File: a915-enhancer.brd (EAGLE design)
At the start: 100 x 50 mm, 74 parts, among them U1 SCREW-M2X8, U10 FX2-20S-1.27DS, U2 SCREW-M2X8, U3 NUT-M2-SELFLOCK, U4 NUT-M2-SELFLOCK, U5 FX2-20P-1.27DS, U6 SCREW-M2X8, U7 SCREW-M2X8, U8 NUT-M2-SELFLOCK, U9 NUT-M2-SELFLOCK

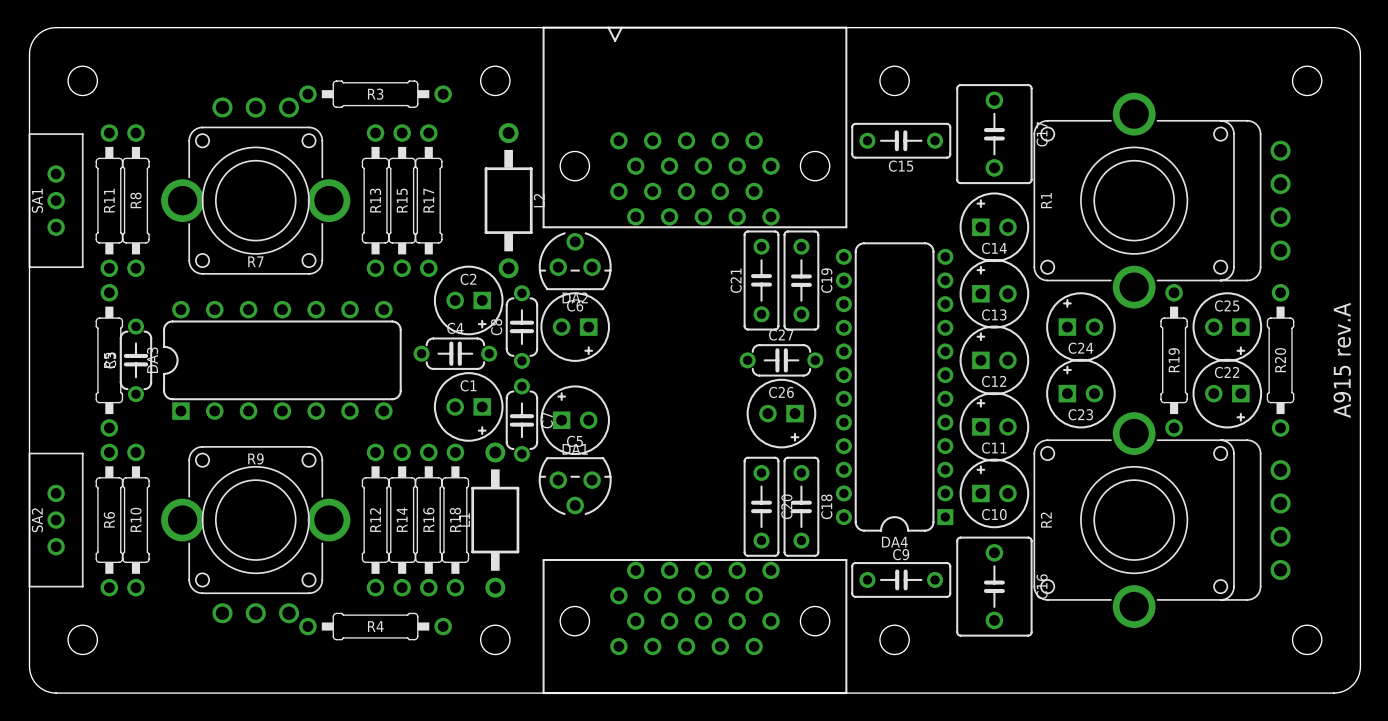
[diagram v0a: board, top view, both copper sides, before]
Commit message: A915a Change component placement
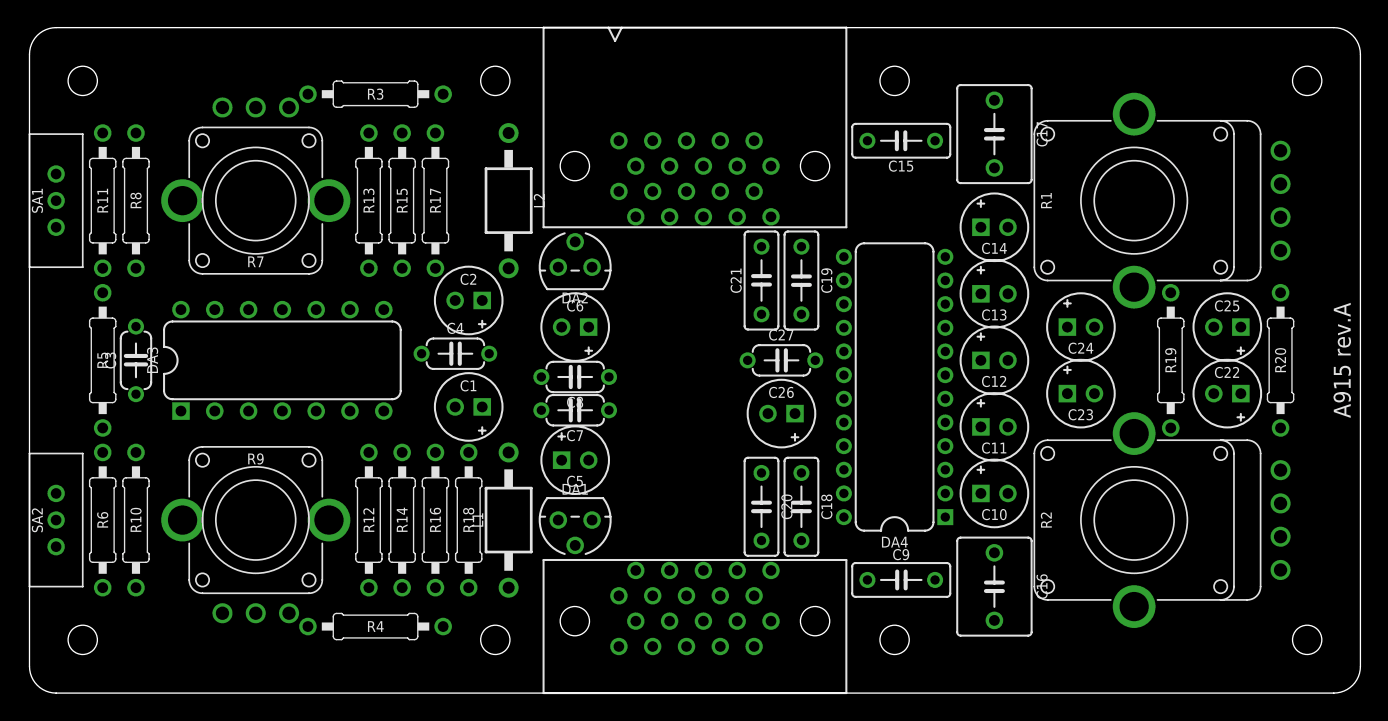
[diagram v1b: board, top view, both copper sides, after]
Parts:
- moved C8 5.48 mm to (41.0, 23.8), turned to 180 degrees
- moved C7 4.07 mm to (41.0, 21.2), turned to 180 degrees
- moved C5 3.00 mm to (41.0, 17.5)
- moved DA1 3.00 mm to (41.0, 13.0)
- moved L1 1.00 mm to (36.0, 13.0)
- moved R18 1.00 mm to (33.0, 13.0)
- moved R11 0.50 mm to (5.50, 37.0)
- moved R12 0.50 mm to (25.5, 13.0)
- moved R13 0.50 mm to (25.5, 37.0)
- moved R16 0.50 mm to (30.5, 13.0)
- moved R17 0.50 mm to (30.5, 37.0)
- moved R5 0.50 mm to (5.50, 25.0)
- moved R6 0.50 mm to (5.50, 13.0)
- moved R19 0.25 mm to (85.8, 25.0)

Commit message: A915a Routing
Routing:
- net -15V: track 0.00 -> 126.4 mm, vias 0 -> 1
- net CV2: track 0.00 -> 121.8 mm, vias 0 -> 1
- net CV1: track 0.00 -> 115.4 mm
- net N$39: track 0.00 -> 72.7 mm
- net -5V: track 0.00 -> 67.0 mm
- net N$10: track 0.00 -> 66.4 mm
- net N$33: track 0.00 -> 57.3 mm
- net N$32: track 0.00 -> 53.2 mm
- net N$42: track 0.00 -> 50.3 mm
- net N$16: track 0.00 -> 48.1 mm
- net DEFINITION: track 0.00 -> 47.9 mm
- net N$41: track 0.00 -> 47.6 mm
- net N$1: track 0.00 -> 46.8 mm
- net N$40: track 0.00 -> 46.0 mm
- net N$44: track 0.00 -> 45.4 mm
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- added copper zone on layer 1, net GND
- added copper zone on layer 16, net GND
